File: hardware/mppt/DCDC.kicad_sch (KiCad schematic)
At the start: 27 parts, among them Q501 EPC2059, Q502 EPC2059

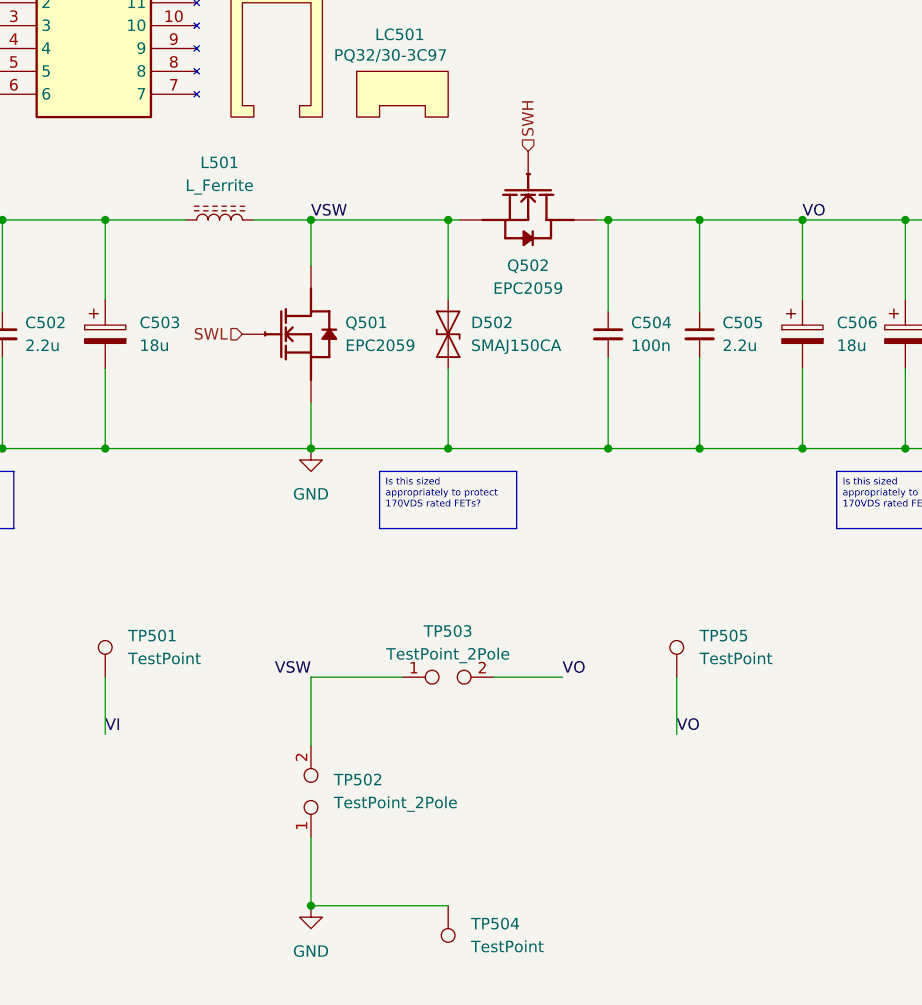
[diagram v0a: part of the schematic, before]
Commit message: run through mppt sch, going through bom
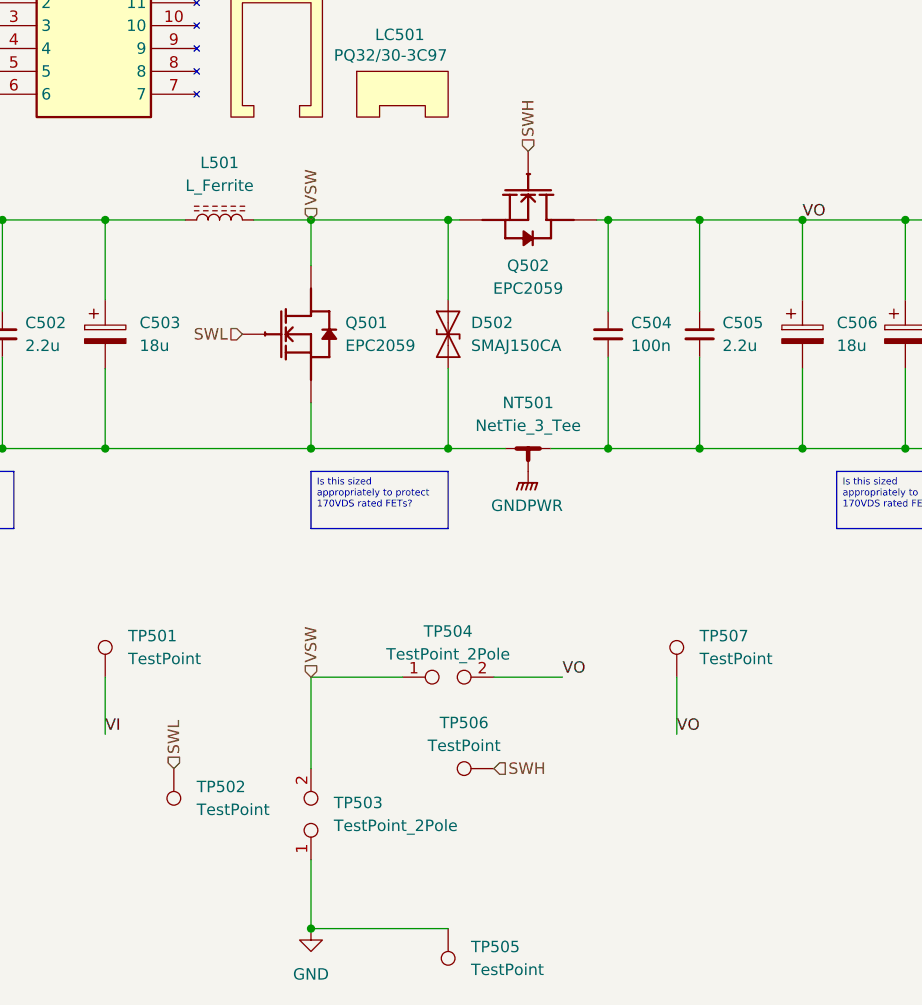
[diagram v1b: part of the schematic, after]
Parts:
- added NT501: NetTie_3_Tee, symbol Device:NetTie_3_Tee
- added TP502, TP506: TestPoint, symbol Connector:TestPoint
- C501, C504: Manufacturer (none) -> Samsung Electro-Mechanics; Notes (none) -> 150V Rating
- C502, C505: Notes (none) -> 150V Rating
- TP501: footprint TestPoint:TestPoint_Keystone_5000-5004_Miniature -> (none); Manufacturer Keystone Electronics -> (none); P/N 5000 -> (none)
- TP505: renamed from TP504; footprint TestPoint:TestPoint_Keystone_5000-5004_Miniature -> (none); Manufacturer Keystone Electronics -> (none); P/N 5000 -> (none)
- TP507: renamed from TP505; footprint TestPoint:TestPoint_Keystone_5000-5004_Miniature -> (none); Manufacturer Keystone Electronics -> (none); P/N 5000 -> (none)
- renumbered TP502 to TP503, TP503 to TP504
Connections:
- net GND: no longer C501.2, C502.2, C503.2, C504.2, C505.2, C506.2, C507.2, D501.2 (A), D502.1 (A1), D503.2 (A), Q501.2 (S), Q501.4 (S), Q501.6 (S)
- net SWH: now also TP506.1
- net SWL: now also TP502.1
- new net GNDPWR: NT501.3
- new net VI-: C501.2, C502.2, C503.2, D501.2 (A), D502.1 (A1), NT501.1, Q501.2 (S), Q501.4 (S), Q501.6 (S)
- new net VO-: C504.2, C505.2, C506.2, C507.2, D503.2 (A), NT501.2
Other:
- moved on the sheet: TP503, TP505

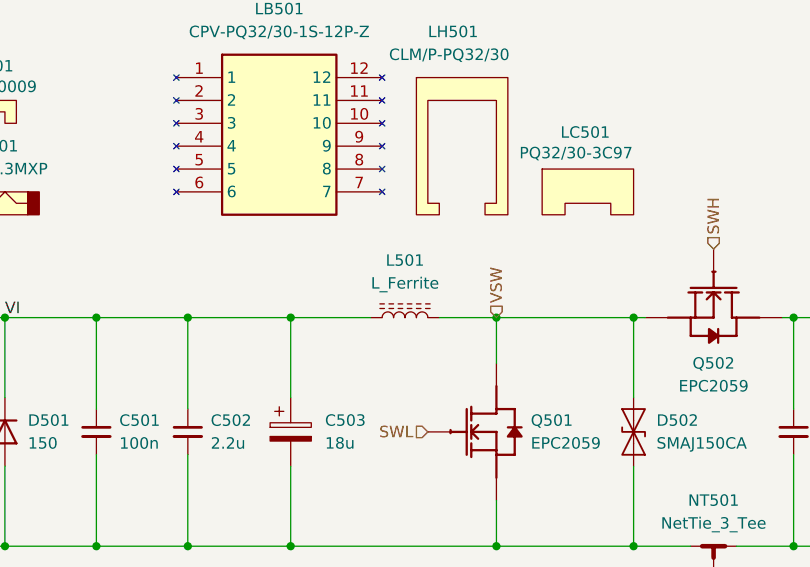
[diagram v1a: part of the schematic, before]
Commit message: update final missing pieces for sch, moving to bom pop
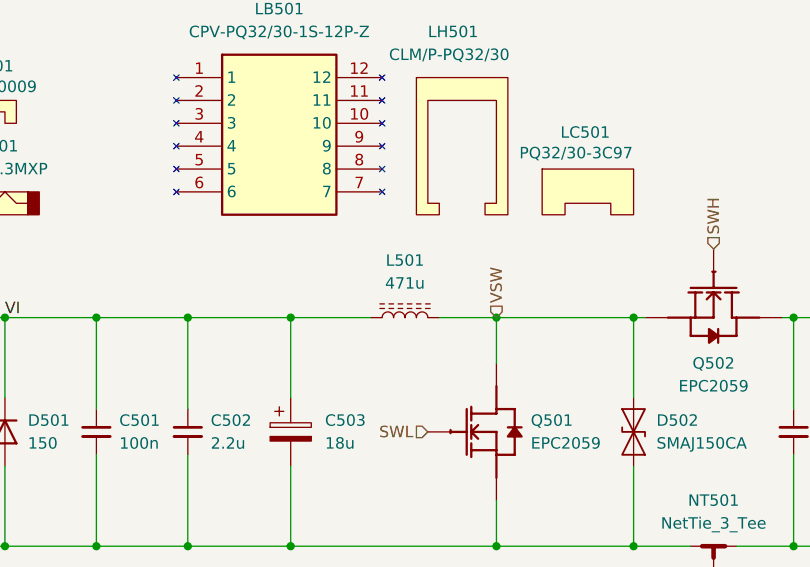
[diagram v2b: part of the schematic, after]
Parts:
- C502, C505: footprint Capacitor_SMD:C_2220_5750Metric_Pad1.97x5.40mm_HandSolder -> (none); P/N CGA9P3X7T2E225M250KA -> (none)
- L501: value L_Ferrite -> 471u
- TP501, TP502, TP505, TP506, TP507: footprint (none) -> TestPoint:TestPoint_Keystone_5000-5004_Miniature; Manufacturer (none) -> Keystone Electronics; P/N (none) -> 5000
- TP503, TP504: footprint (none) -> TestPoint:TestPoint_2Pads_Pitch2.54mm_Drill0.8mm
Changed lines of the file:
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@@
 			)
 		)
-		(property "Footprint" ""
+		(property "Footprint" "TestPoint:TestPoint_Keystone_5000-5004_Miniature"
 			(at 119.38 167.64 0)
 			(effects
@@
 			)
 		)
-		(property "Datasheet" "~"
+		(property "Datasheet" "https://www.keyelco.com/userAssets/file/M65p56.pdf"
 			(at 119.38 167.64 0)
 			(effects
@@
 			)
 		)
+		(property "Manufacturer" "Keystone Electronics"
+			(at 119.38 162.56 0)
+			(effects
+				(font
+					(size 1.27 1.27)
+				)
+				(hide yes)
+			)
+		)
+		(property "P/N" "5000"
+			(at 119.38 162.56 0)
+			(effects
+				(font
+					(size 1.27 1.27)
+				)
+				(hide yes)
+			)
+		)
 		(pin "1"
 		)
@@
 			)
 		)
-		(property "Footprint" ""
+		(property "Footprint" "TestPoint:TestPoint_2Pads_Pitch2.54mm_Drill0.8mm"
 			(at 114.3 152.4 0)
 			(effects
@@
 			)
 		)
-		(property "Footprint" ""
+		(property "Footprint" "TestPoint:TestPoint_Keystone_5000-5004_Miniature"
 			(at 78.74 162.56 0)
 			(effects
@@
 			)
 		)
-		(property "Datasheet" "~"
+		(property "Datasheet" "https://www.keyelco.com/userAssets/file/M65p56.pdf"
 			(at 78.74 162.56 0)
 			(effects
@@
 			)
 		)
+		(property "Manufacturer" "Keystone Electronics"
+			(at 83.82 162.56 0)
+			(effects
+				(font
+					(size 1.27 1.27)
+				)
+				(hide yes)
+			)
+		)
+		(property "P/N" "5000"
+			(at 83.82 162.56 0)
+			(effects
+				(font
+					(size 1.27 1.27)
+				)
+				(hide yes)
+			)
+		)
 		(pin "1"
 		)
@@
 			)
 		)
-		(property "Footprint" ""
+		(property "Footprint" "TestPoint:TestPoint_2Pads_Pitch2.54mm_Drill0.8mm"
 			(at 99.06 167.64 0)
 			(effects
@@
 			)
 		)
-		(property "Value" "L_Ferrite"
+		(property "Value" "471u"
 			(at 88.9 97.79 90)
 			(effects
@@
 			)
 		)
-		(property "Footprint" ""
+		(property "Footprint" "TestPoint:TestPoint_Keystone_5000-5004_Miniature"
 			(at 81.28 152.4 0)
 			(effects
@@
 			)
 		)
-		(property "Datasheet" ""
+		(property "Datasheet" "https://www.keyelco.com/userAssets/file/M65p56.pdf"
 			(at 81.28 152.4 0)
 			(effects
@@
 			)
 		)
-		(property "Manufacturer" ""
+		(property "Manufacturer" "Keystone Electronics"
 			(at 76.2 152.4 0)
 			(effects
@@
 			)
 		)
-		(property "P/N" ""
+		(property "P/N" "5000"
 			(at 76.2 152.4 0)
 			(effects
@@
 			)
 		)
-		(property "Footprint" "Capacitor_SMD:C_2220_5750Metric_Pad1.97x5.40mm_HandSolder"
+		(property "Footprint" ""
 			(at 64.77 114.3 0)
 			(effects
@@
 			)
 		)
-		(property "Datasheet" "https://product.tdk.com/en/system/files?file=dam/doc/product/capacitor/ceramic/mlcc/catalog/mlcc_automotive_midvoltage_en.pdf"
+		(property "Datasheet" ""
 			(at 64.77 114.3 0)
 			(effects
@@
 			)
 		)
-		(property "P/N" "CGA9P3X7T2E225M250KA"
+		(property "P/N" ""
 			(at 64.77 114.3 0)
 			(effects
@@
 			)
 		)
-		(property "Footprint" ""
+		(property "Footprint" "TestPoint:TestPoint_Keystone_5000-5004_Miniature"
 			(at 109.22 180.34 0)
 			(effects
@@
 			)
 		)
-		(property "Datasheet" ""
+		(property "Datasheet" "https://www.keyelco.com/userAssets/file/M65p56.pdf"
 			(at 109.22 180.34 0)
 			(effects
@@
 			)
 		)
-		(property "Manufacturer" ""
+		(property "Manufacturer" "Keystone Electronics"
 			(at 114.3 180.34 0)
 			(effects
@@
 			)
 		)
-		(property "P/N" ""
+		(property "P/N" "5000"
 			(at 114.3 180.34 0)
 			(effects
@@
 			)
 		)
-		(property "Footprint" ""
+		(property "Footprint" "TestPoint:TestPoint_Keystone_5000-5004_Miniature"
 			(at 144.78 152.4 0)
 			(effects
@@
 			)
 		)
-		(property "Datasheet" ""
+		(property "Datasheet" "https://www.keyelco.com/userAssets/file/M65p56.pdf"
 			(at 144.78 152.4 0)
 			(effects
@@
 			)
 		)
-		(property "Manufacturer" ""
+		(property "Manufacturer" "Keystone Electronics"
 			(at 139.7 152.4 0)
 			(effects
@@
 			)
 		)
-		(property "P/N" ""
+		(property "P/N" "5000"
 			(at 139.7 152.4 0)
 			(effects
@@
 			)
 		)
-		(property "Footprint" "Capacitor_SMD:C_2220_5750Metric_Pad1.97x5.40mm_HandSolder"
+		(property "Footprint" ""
 			(at 142.24 114.3 0)
 			(effects
@@
 			)
 		)
-		(property "Datasheet" "https://product.tdk.com/en/system/files?file=dam/doc/product/capacitor/ceramic/mlcc/catalog/mlcc_automotive_midvoltage_en.pdf"
+		(property "Datasheet" ""
 			(at 142.24 114.3 0)
 			(effects
@@
 			)
 		)
-		(property "P/N" "CGA9P3X7T2E225M250KA"
+		(property "P/N" ""
 			(at 142.24 114.3 0)
 			(effects
@@
 			)
 		)
-		(property "Datasheet" "~"
+		(property "Datasheet" ""
 			(at 123.19 127 0)
 			(effects

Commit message: bom consolidated, starting layout
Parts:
- removed C504: 100n, symbol Device:C_Small
- added C503, C507: 2.2u, Capacitor_SMD:C_2220_5750Metric_Pad1.97x5.40mm_HandSolder, symbol Device:C_Small
- added C505: 100n, Capacitor_SMD:C_1206_3216Metric_Pad1.33x1.80mm_HandSolder, symbol Device:C_Small
- C501: footprint (none) -> Capacitor_SMD:C_1206_3216Metric_Pad1.33x1.80mm_HandSolder; Manufacturer Samsung Electro-Mechanics -> TDK; Notes 150V Rating -> 85V Rating; P/N (none) -> CGA5L3X7R2E104K160AA
- C502: value 2.2u -> 1u; footprint (none) -> Capacitor_SMD:C_2220_5750Metric_Pad1.97x5.40mm_HandSolder; P/N (none) -> CGA9N3X7R2E105K230KA
- C504: renamed from C503; Notes (none) -> 150V Rating
- C506: renamed from C505; value 2.2u -> 1u; footprint (none) -> Capacitor_SMD:C_2220_5750Metric_Pad1.97x5.40mm_HandSolder; P/N (none) -> CGA9N3X7R2E105K230KA
- C508: renamed from C506; Notes (none) -> 150V Rating
- C509: renamed from C507; Notes (none) -> 150V Rating
- D501, D503: footprint Diode_SMD:D_SMA -> Diode_SMD:D_SMA_Handsoldering
- D502: footprint Diode_SMD:D_SMA -> Diode_SMD:D_SMA_Handsoldering; Manufacturer Littelfuse -> Diodes Incorporated; P/N SMAJ150CA -> SMAJ150CA-13-F
- NT501: footprint (none) -> NetTie:NetTie-3_SMD_Pad2.0mm
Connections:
- net VI: now also C503.1
- net VI-: now also C503.2
- net VO: now also C505.1, C507.1
- net VO-: now also C505.2, C507.2
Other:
- moved on the sheet: C504, C506, C508, C509, D501, D502, D503, F501, F502, FC501, FC502, FX501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

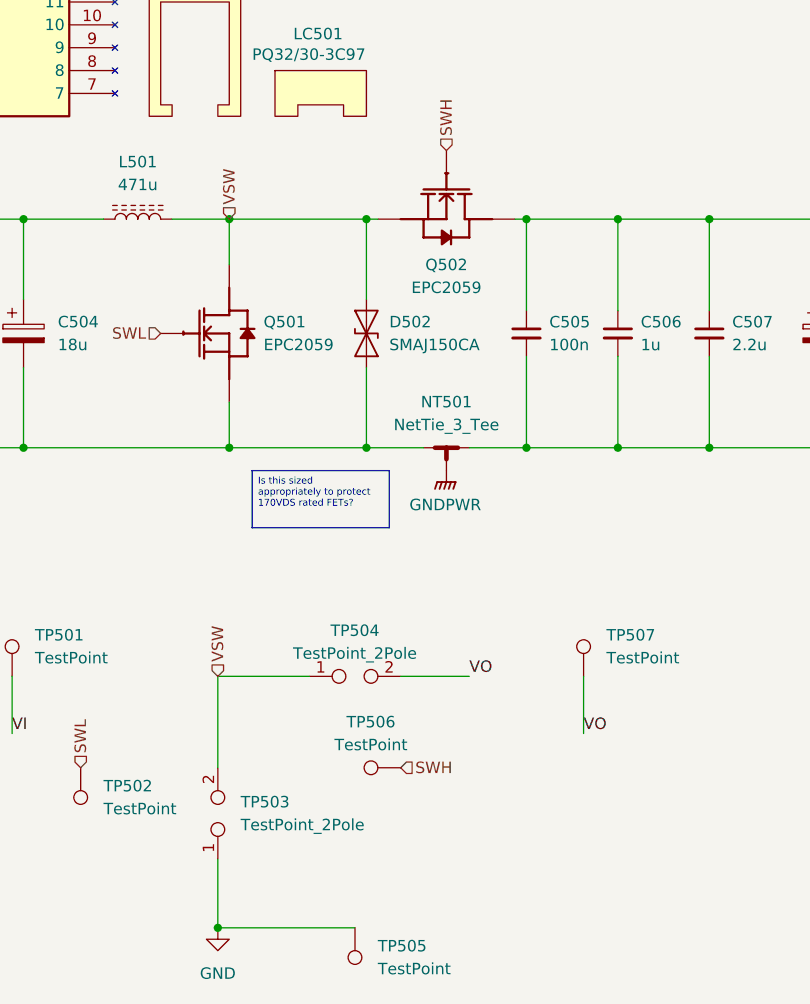
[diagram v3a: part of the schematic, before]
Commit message: placement of majority of power path
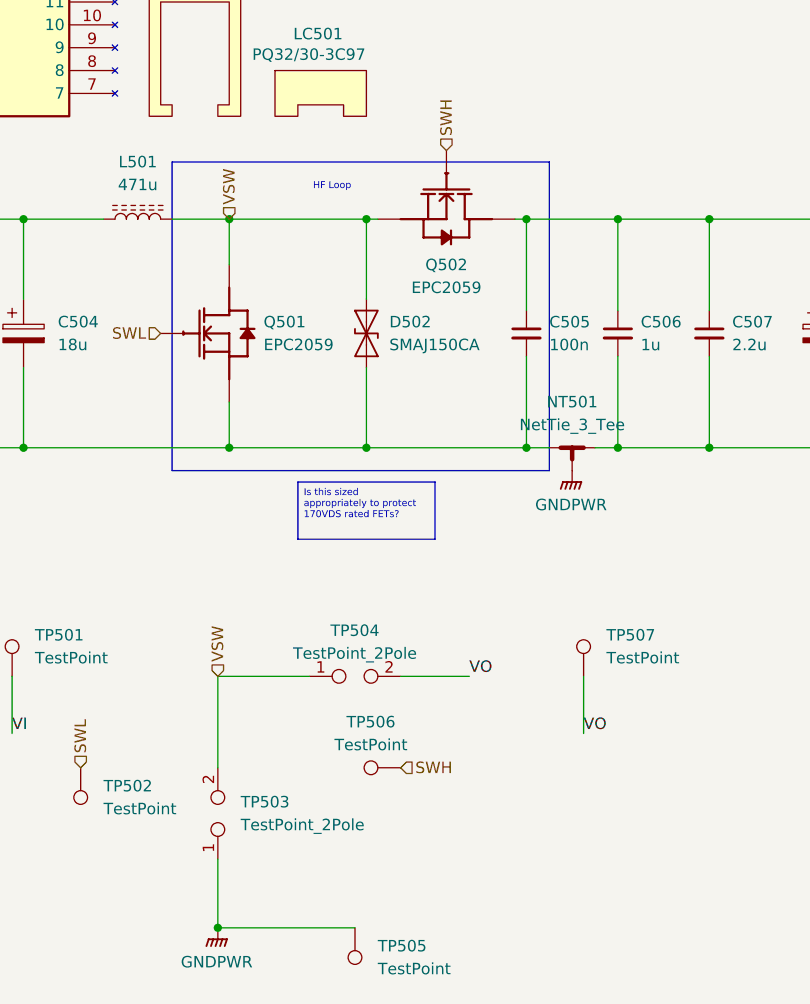
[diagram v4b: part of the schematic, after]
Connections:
- net GND is gone; now on net GNDPWR: TP503.1, TP505.1
- net VI-: now also C505.2
- net VO-: no longer C505.2
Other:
- note added: "HF Loop"
